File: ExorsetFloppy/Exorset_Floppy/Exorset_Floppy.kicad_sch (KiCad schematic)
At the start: 19 parts, among them J1 BUS, U2 GAL16V8, U3 74HC245

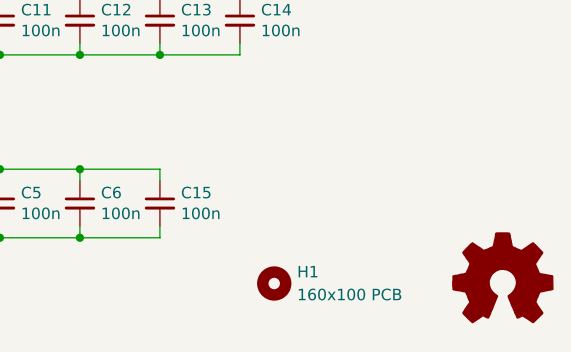
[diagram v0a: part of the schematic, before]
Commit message: Exorset Floppy added
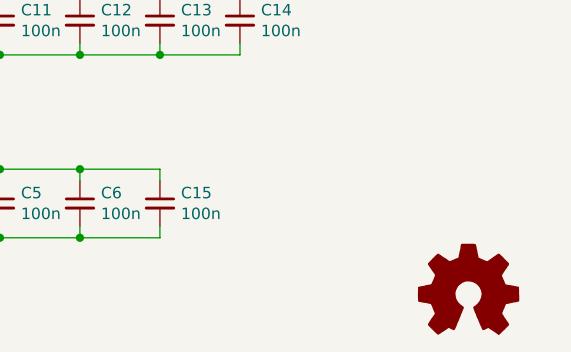
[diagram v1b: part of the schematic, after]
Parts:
- removed H1: 160x100 PCB, my_own:Eurocard_160x100_19inch_holes_connector, symbol Mechanical:MountingHole
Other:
- title: CPU09RAM -> Exorset Floppy
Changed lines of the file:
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@@
 	(paper "A3")
 	(title_block
-		(title "CPU09RAM")
-		(date "2025-03-19")
+		(title "Exorset Floppy")
+		(date "2025-08-22")
 		(rev "v0.1")
 		(company "100% Offner")
-		(comment 1 "kees1948 UniFLEX System SMD Version")
+		(comment 1 "Exorset Floppy Controller for kees1948 UniFLEX System")
 		(comment 2 "v0.1:Initial")
 	)
@@
 	(symbol
 		(lib_id "Graphic:Logo_Open_Hardware_Small")
-		(at 400.05 245.11 0)
+		(at 396.24 246.38 0)
 		(unit 1)
 		(exclude_from_sim yes)
@@
 		(fields_autoplaced yes)
 		(property "Reference" "#SYM1"
-			(at 400.05 238.125 0)
+			(at 396.24 239.395 0)
 			(effects
 				(font
@@
 		)
 		(property "Value" "Logo_Open_Hardware_Small"
-			(at 400.05 250.825 0)
+			(at 396.24 252.095 0)
 			(effects
 				(font
@@
 		)
 		(property "Footprint" ""
-			(at 400.05 245.11 0)
+			(at 396.24 246.38 0)
 			(effects
 				(font
@@
 		)
 		(property "Datasheet" "~"
-			(at 400.05 245.11 0)
+			(at 396.24 246.38 0)
 			(effects
 				(font
@@
 		)
 		(property "Description" "Open Hardware logo, small"
-			(at 400.05 245.11 0)
+			(at 396.24 246.38 0)
 			(effects
 				(font
@@
 					(unit 1)
 				)
-			)
-		)
-	)
-	(symbol
-		(lib_id "Mechanical:MountingHole")
-		(at 374.65 245.11 0)
-		(unit 1)
-		(exclude_from_sim yes)
-		(in_bom no)
-		(on_board yes)
-		(dnp no)
-		(fields_autoplaced yes)
-		(property "Reference" "H1"
-			(at 377.19 243.8399 0)
-			(effects
-				(font
-					(size 1.27 1.27)
-				)
-				(justify left)
-			)
-		)
-		(property "Value" "160x100 PCB"
-			(at 377.19 246.3799 0)
-			(effects
-				(font
-					(size 1.27 1.27)
-				)
-				(justify left)
-			)
-		)
-		(property "Footprint" "my_own:Eurocard_160x100_19inch_holes_connector"
-			(at 374.65 245.11 0)
-			(effects
-				(font
-					(size 1.27 1.27)
-				)
-				(hide yes)
-			)
-		)
-		(property "Datasheet" "~"
-			(at 374.65 245.11 0)
-			(effects
-				(font
-					(size 1.27 1.27)
-				)
-				(hide yes)
-			)
-		)
-		(property "Description" "Mounting Hole without connection"
-			(at 374.65 245.11 0)
-			(effects
-				(font
-					(size 1.27 1.27)
-				)
-				(hide yes)
-			)
-		)
-		(instances
-			(project ""
-				(path "/05fb24d5-db99-47c3-b50e-9b588fa507ac"
-					(reference "H1")
-					(unit 1)
-				)

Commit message: Exordisk first version
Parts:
- removed C10, C11, C12, C13, C14, C7, C8, C9: 100n, Capacitor_SMD:C_1206_3216Metric_Pad1.33x1.80mm_HandSolder, symbol Device:C_Small
- removed U2: GAL16V8, Package_DIP:DIP-20_W7.62mm_Socket, symbol Logic_Programmable:GAL16V8
- added U1: GAL22V10, Package_DIP:DIP-24_W7.62mm, symbol my_ics_new:GAL22V10
- added U14: 74HCT74, Package_DIP:DIP-14_W7.62mm, symbol 74xx:74LS74
- added U6: 27C32, Package_DIP:DIP-24_W15.24mm, symbol my_ics_new:27C32
- C1: footprint Capacitor_Tantalum_SMD:CP_EIA-7343-31_Kemet-D_Pad2.25x2.55mm_HandSolder -> Capacitor_Tantalum_SMD:CP_EIA-7343-31_Kemet-D_HandSolder
- U3: footprint Package_SO:SOIC-20W_7.5x12.8mm_P1.27mm -> Package_DIP:DIP-20_W7.62mm
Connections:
- net ID0 is gone; now on net BD7: U3.9 (A7)
- net ID1 is gone; now on net BD6: U3.8 (A6)
- net ID2 is gone; now on net BD5: U3.7 (A5)
- net ID3 is gone; now on net BD4: U3.6 (A4)
- net ID4 is gone; now on net BD3: U3.5 (A3)
- net ID5 is gone; now on net BD2: U3.4 (A2)
- net ID6 is gone; now on net BD1: U3.3 (A1)
- net ID7 is gone; now on net BD0: U3.2 (A0)
- net +5V: now also U1.24 (VCC), U14.1 (~{R}), U14.4 (~{S}), U6.24 (VCC)
- net BA0: now also U6.8 (A0)
- net BA1: now also U6.7 (A1)
- net BA10: now also U1.9 (I9), U6.19 (A10)
- net BA11: now also U1.8 (I8), U6.21 (A11)
- net BA12: now also U1.7 (I7)
- net BA13: now also U1.6 (I6)
- net BA14: now also U1.5 (I5)
- net BA15: now also U1.4 (I4)
- net BA2: now also U1.18 (IO6), U6.6 (A2)
- net BA3: now also U1.17 (IO7), U6.5 (A3)
- net BA4: now also U1.16 (IO8), U6.4 (A4)
- net BA5: now also U1.15 (IO9), U6.3 (A5)
- net BA6: now also U1.14 (IO10), U6.2 (A6)
- net BA7: now also U1.13 (IO11), U6.1 (A7)
- net BA8: now also U1.11 (I11), U6.23 (A8)
- net BA9: now also U1.10 (I10), U6.22 (A9)
- net BD0: no longer U3.11 (B7)
- net BD1: no longer U3.12 (B6)
- net BD2: no longer U3.13 (B5)
- net BD3: no longer U3.14 (B4)
- net BD4: no longer U3.15 (B3)
- net BD5: no longer U3.16 (B2)
- net BD6: no longer U3.17 (B1)
- net BD7: no longer U3.18 (B0)
- net B_E: now also U1.2 (I2), U14.3 (C)
- net DBDIR: now also U1.22 (IO2)
- net GND: now also U1.12 (GND), U6.12 (GND), U6.18 (~{CE})
- net ~{B_RW}: now also U1.3 (I3)
- net ~{B_VMA}: now also U1.1 (I1/CLK)
- net ~{DBEN}: now also U1.23 (IO1)
- net ~{B_IRQ} renamed ~{IRQ}
- net ~{B_NMI} renamed ~{NMI}
- new net: U14.2 (D), U14.6 (~{Q})
- new net D0: U3.18 (B0), U6.9 (D0)
- new net D1: U3.17 (B1), U6.10 (D1)
- new net D2: U3.16 (B2), U6.11 (D2)
- new net D3: U3.15 (B3), U6.13 (D3)
- new net D4: U3.14 (B4), U6.14 (D4)
- new net D5: U3.13 (B5), U6.15 (D5)
- new net D6: U3.12 (B6), U6.16 (D6)
- new net D7: U3.11 (B7), U6.17 (D7)
- new net Floppy Logic/CLK500k: U14.5 (Q)
- new net ~{6820_CS}: U1.20 (IO4)
- new net ~{6852_CS}: U1.21 (IO3)
- new net ~{ROM_CS}: U1.19 (IO5), U6.20 (~{OE}/VPP)
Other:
- added sheet Floppy Logic (floppyLogic.kicad_sch)
- note added: "E800-EBFF"
- note added: "EC00-EC03"
- note added: "EC04-EC07"

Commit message: Board finished, GALS added
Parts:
- added J4, J5, J6: Conn_01x01, Connector_PinHeader_1.27mm:PinHeader_1x01_P1.27mm_Vertical, symbol Connector_Generic:Conn_01x01
- added U11, U12, U16, U18, U2: 74HCT74, Package_DIP:DIP-14_W7.62mm, symbol 74xx:74LS74
- added U15: 74HCT04, Package_DIP:DIP-14_W7.62mm, symbol 74xx:74LS04
- added U17: 74HCT00, Package_DIP:DIP-14_W7.62mm, symbol 74xx:74LS00
- added U19: 74LS76, Package_DIP:DIP-16_W7.62mm, symbol 74xx:74LS76
- added U23: 74LS123, Package_DIP:DIP-16_W7.62mm, symbol 74xx:74LS123
- added U25: 74LS04, Package_DIP:DIP-14_W7.62mm, symbol 74xx:74LS04
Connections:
- net +5V: now also U11.14 (VCC), U12.14 (VCC), U15.14 (VCC), U16.14 (VCC), U17.14 (VCC), U18.14 (VCC), U19.5 (VCC), U2.14 (VCC), U23.16 (VCC), U25.14 (VCC)
- net BA11: no longer U1.8 (I8)
- net BA12: no longer U1.7 (I7)
- net BA13: no longer U1.6 (I6)
- net BA14: no longer U1.5 (I5)
- net BA15: no longer U1.4 (I4)
- net BA2: now also U1.6 (I6); no longer U1.18 (IO6)
- net BA3: now also U1.5 (I5); no longer U1.17 (IO7)
- net BA4: now also U1.7 (I7); no longer U1.16 (IO8)
- net B_BA: now also U1.8 (I8)
- net GND: now also U11.7 (GND), U12.7 (GND), U15.7 (GND), U16.7 (GND), U17.7 (GND), U18.7 (GND), U19.13 (GND), U2.7 (GND), U23.8 (GND), U25.7 (GND)
- new net: J6.1 (Pin_1), U1.18 (IO6)
- new net: J4.1 (Pin_1), U1.16 (IO8)
- new net: J5.1 (Pin_1), U1.17 (IO7)
- new net SEL: U1.4 (I4)
- no-connect marks 7 -> 14
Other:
- sheet Floppy Logic ports: added BA[0..15], SEL; removed none

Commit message: some small adjustments
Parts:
- added JP8: CLOCKSRC, Jumper:SolderJumper-3_P1.3mm_Bridged12_RoundedPad1.0x1.5mm_NumberLabels, symbol Jumper:SolderJumper_3_Bridged12
- added Y1: 1M, Oscillator:Oscillator_DIP-8, symbol Oscillator:CXO_DIP8
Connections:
- net +5V: now also Y1.1 (EN), Y1.8 (Vcc)
- net B_E: now also JP8.1 (A); no longer U14.3 (C)
- net GND: now also Y1.4 (GND)
- new net: JP8.2 (C), U14.3 (C)
- new net: JP8.3 (B), Y1.5 (OUT)

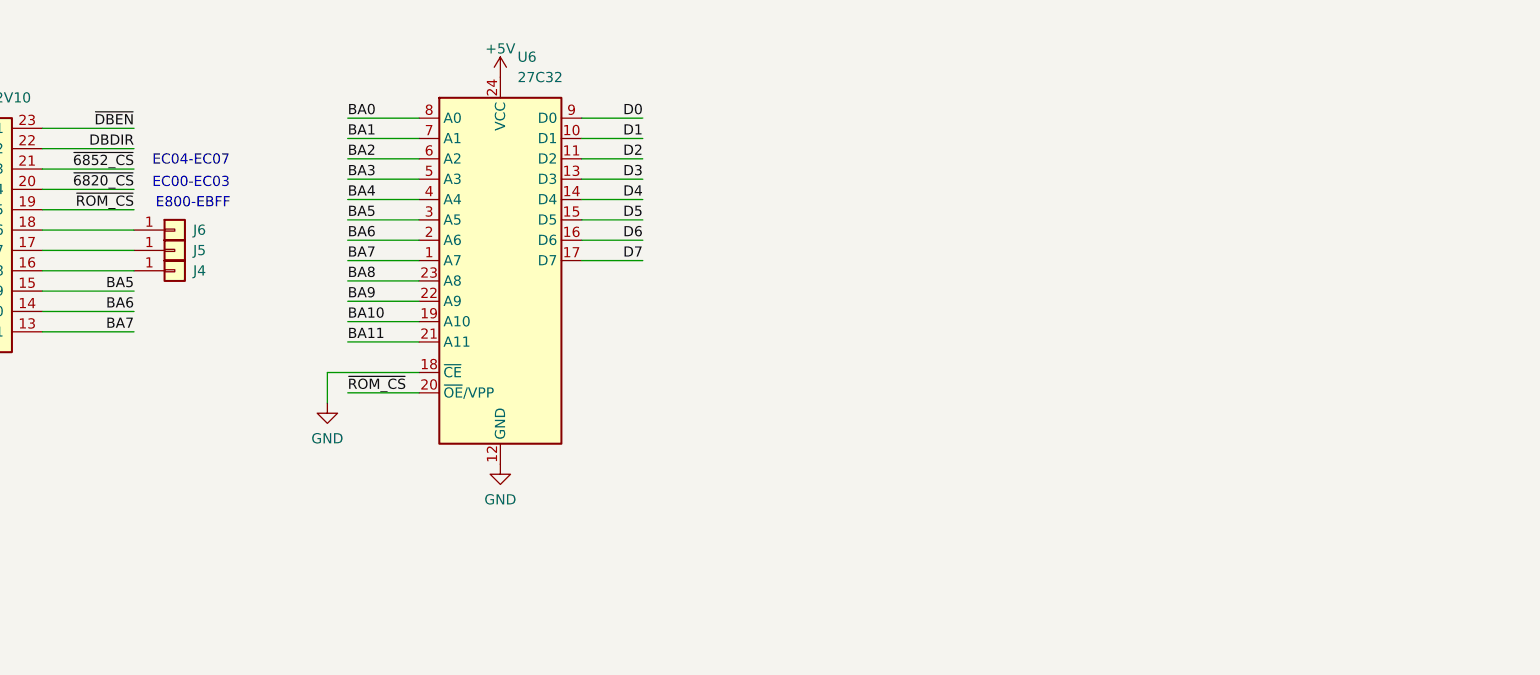
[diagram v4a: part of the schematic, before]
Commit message: new GAL eq. for additional EPROM on board
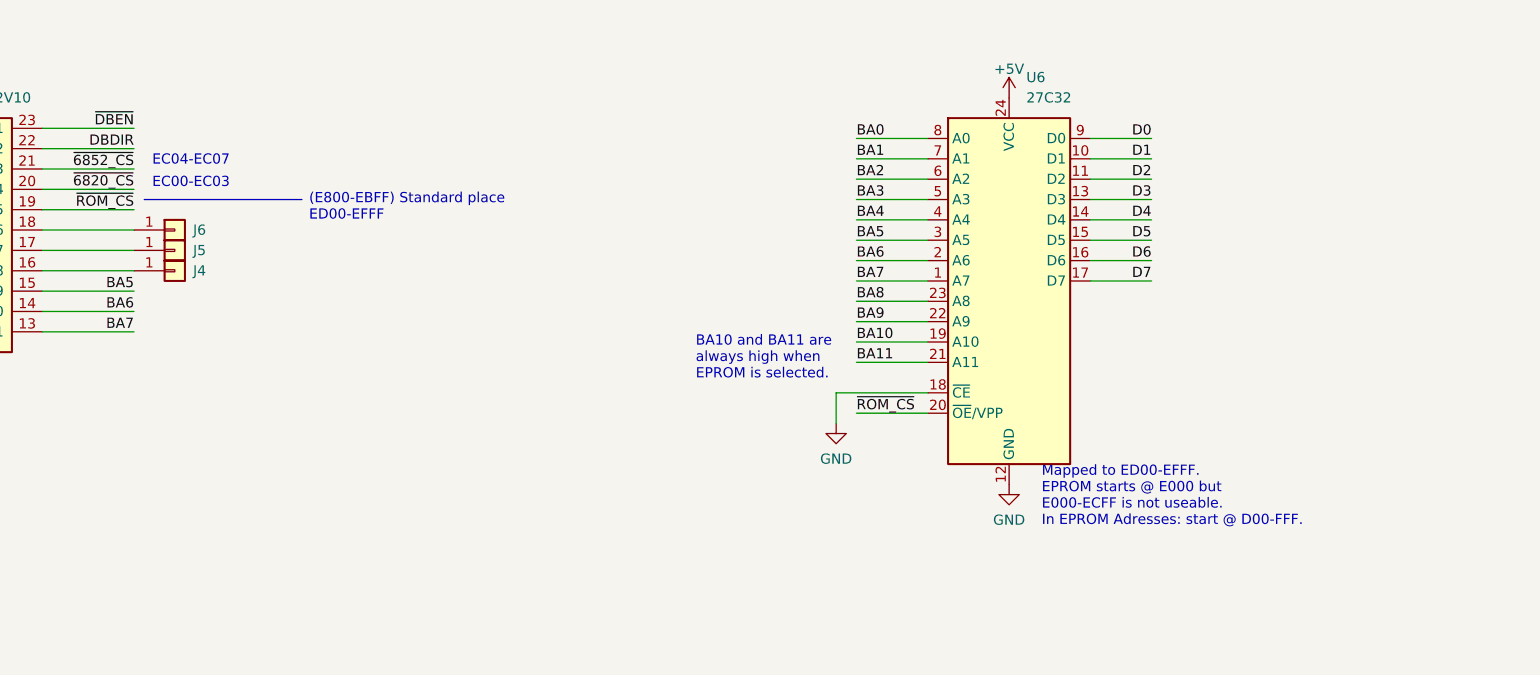
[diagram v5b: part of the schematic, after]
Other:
- note added: "(E800-EBFF) Standard place ED00-EFFF"
- note added: "BA10 and BA11 are always high when EPROM is selected."
- note added: "Mapped to ED00-EFFF. EPROM starts @ E000 but E000-ECFF is not useable. In EPROM Adresses: start @ D00-FFF."
- note removed: "E800-EBFF"
- moved on the sheet: U6
